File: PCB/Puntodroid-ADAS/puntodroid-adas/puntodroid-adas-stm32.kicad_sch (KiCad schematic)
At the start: 6 parts, among them J1 USB_B, J2 BOOTLOADER, J3 SWD_INTERFACE, U1 STM32F446VETx

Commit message: UPDATE cube mx
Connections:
- net CAN_LS_FAULT: no longer U1.83 (PD2)
- net SWCLK: now also U1.76 (PA14)
- net SWDIO: now also U1.72 (PA13)
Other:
- note added: "SPI1_MISO"
- note added: "SPI1_MOSI"
- note added: "SPI1_NSS"
- note added: "SPI1_SCK"

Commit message: update puntodroid
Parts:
- removed J3: SWD_INTERFACE, symbol Connector_Generic:Conn_01x06
- added C1, C2: 22p, symbol Device:C
- added C10, C12, C13, C5, C6, C7, C8, C9: 100n, symbol Device:C
- added C3, C4: 2u2, symbol Device:C_Polarized
- added J3: SWD PROGRAMMER, symbol Connector_Generic:Conn_01x05
- added R3: 5k6, symbol Device:R
- added R4, R5: 10k, symbol Device:R
- added U2: CM1293A, Package_TO_SOT_SMD:SOT-23-6, symbol Power_Protection:CDSOT236-0504C
- added Y1: 16MHz, symbol Device:Crystal
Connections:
- net +3V3: now also J2.1 (Pin_1), C10.2, C12.2, C13.2, C5.2, C6.2, C7.2, C8.2, C9.2, J3.2 (Pin_2), U2.5 (VP); no longer J2.6 (Pin_6)
- net BOOT0: now also J2.5 (Pin_5); no longer J2.2 (Pin_2)
- net BOOTLOADER_RX: now also J2.3 (Pin_3); no longer J2.4 (Pin_4)
- net BOOTLOADER_TX: now also J2.2 (Pin_2); no longer J2.5 (Pin_5)
- net CAN_LS_FAULT: now also U1.96 (PB9); no longer U1.53 (PB14)
- net CAN_LS_RX: now also U1.52 (PB13); no longer U1.51 (PB12)
- net CAN_LS_TX: now also U1.51 (PB12); no longer U1.52 (PB13)
- net DS18B20: now also U1.83 (PD2); no longer U1.24 (PA1)
- net GNDD: now also J2.6 (Pin_6), C1.1, C10.1, C12.1, C13.1, C2.1, C3.2, C4.2, C5.1, C6.1, C7.1, C8.1, C9.1, J3.3 (Pin_3), R4.2, R5.2, U2.2 (VN); no longer J2.1 (Pin_1)
- net NRST: now also J2.4 (Pin_4), J3.1 (Pin_1); no longer J2.3 (Pin_3)
- net PUSH_BUTTON_1: now also U1.5 (PE6); no longer U1.84 (PD3)
- net PUSH_BUTTON_2: now also U1.15 (PC0); no longer U1.85 (PD4)
- net PUSH_BUTTON_3: now also U1.16 (PC1); no longer U1.86 (PD5)
- net PUSH_BUTTON_4: now also U1.17 (PC2); no longer U1.87 (PD6)
- net PUSH_BUTTON_5: now also U1.18 (PC3); no longer U1.88 (PD7)
- net SWCLK: now also J3.5 (Pin_5)
- net SWDIO: now also J3.4 (Pin_4)
- net USB_D+: now also U2.4 (IO3), U2.6 (IO4)
- net USB_D-: now also U2.1 (IO1), U2.3 (IO2)
- net USB_VBUS: now also R3.2, R4.1; no longer J1.1 (VBUS)
- net VIDEO_MUX_A1: now also U1.36 (PB1); no longer U1.25 (PA2), U1.26 (PA3)
- net PE2_UNUSED: now reaches U1.1 (PE2)
- net at U1.12 (PH0): now also C1.2, Y1.2
- net at U1.13 (PH1): now also C2.2, Y1.1
- net PE3_UNUSED: now reaches U1.2 (PE3)
- net ADC_VBATT_12V: now reaches U1.23 (PA0)
- net PE4_UNUSED: now reaches U1.3 (PE4)
- net at U1.37 (PB2): now also R5.1
- net VIDEO_MUX_A2: now reaches U1.38 (PE7)
- net PE8_UNUSED: now reaches U1.39 (PE8)
- net PUSH_BUTTON_0: now reaches U1.4 (PE5)
- net PE9_UNUSED: now reaches U1.40 (PE9)
- net P10_UNUSED: now reaches U1.41 (PE10)
- net PE11_UNUSED: now reaches U1.42 (PE11)
- net PE12_UNUSED: now reaches U1.43 (PE12)
- net PE13_UNUSED: now reaches U1.44 (PE13)
- net PE14_UNUSED: now reaches U1.45 (PE14)
- net RFM69_CS: now reaches U1.46 (PE15)
- net RFM69_SCK: now reaches U1.47 (PB10)
- net at U1.48 (VCAP_1): now also C4.1
- net RFM69_MISO: now reaches U1.54 (PB15)
- net PD8_UNUSED: now reaches U1.55 (PD8)
- net PD9_UNUSED: now reaches U1.56 (PD9)
- net PD10_UNUSED: now reaches U1.57 (PD10)
- net PD11_UNUSED: now reaches U1.58 (PD11)
- net PD12_UNUSED: now reaches U1.59 (PD12)
- net PD13_UNUSED: now reaches U1.60 (PD13)
- net PD14_UNUSED: now reaches U1.61 (PD14)
- net PD15_UNUSED: now reaches U1.62 (PD15)
- net PC6_UNUSED: now reaches U1.63 (PC6)
- net PC7_UNUSED: now reaches U1.64 (PC7)
- net PC8_UNUSED: now reaches U1.65 (PC8)
- net PC9_UNUSED: now reaches U1.66 (PC9)
- net PA8_UNUSED: now reaches U1.67 (PA8)
- net PA10_UNUSED: now reaches U1.69 (PA10)
- net PC13_UNUSED: now reaches U1.7 (PC13)
- net at U1.73 (VCAP_2): now also C3.1
- net BOOTLOADER_DEBUG_RX: now reaches U1.78 (PC10)
- net BOOTLOADER_DEBUG_TX: now reaches U1.79 (PC11)
- net PC14_UNUSED: now reaches U1.8 (PC14)
- net PC12_UNUSED: now reaches U1.80 (PC12)
- net PB3_UNUSED: now reaches U1.89 (PB3)
- net PC15_UNUSED: now reaches U1.9 (PC15)
- net PB4_UNUSED: now reaches U1.90 (PB4)
- net PB5_UNUSED: now reaches U1.91 (PB5)
- net PB6_UNUSED: now reaches U1.92 (PB6)
- net PB7_UNUSED: now reaches U1.93 (PB7)
- net PB8_UNUSED: now reaches U1.95 (PB8)
- net PE0_UNUSED: now reaches U1.97 (PE0)
- net PE1_UNUSED: now reaches U1.98 (PE1)
- new net: J1.1 (VBUS), R3.1
- new net ADC_5V: U1.24 (PA1)
- new net BUZZER_OUT: U1.84 (PD3)
- new net LPGTECH_RX: U1.25 (PA2)
- new net LPGTECH_TX: U1.26 (PA3)
- new net PD5_UNUSED: U1.86 (PD5)
- new net PD6_UNUSED: U1.87 (PD6)
- new net PD7_UNUSED: U1.88 (PD7)
- new net REVERSE_SIGNAL: U1.85 (PD4)
- new net RFM69_MOSI: U1.53 (PB14)
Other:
- note added: "16MHz CRYSTAL"
- note added: "ADC_IN0"
- note added: "ADC_IN1"
- note added: "BOOT1 configuration"
- note added: "BOOTLOADER DEBUG UART"
- note added: "CAN2_RX"
- note added: "CAN2_TX"
- note added: "RCC_OSC_IN"
- note added: "RCC_OSC_OUT"
- note added: "SPI2_MISO"
- note added: "SPI2_MOSI"
- note added: "SPI2_SCK"
- note added: "SWD PROGRAMMING"
- note added: "USART2_RX"
- note added: "USART2_TX"
- note added: "USART3_RX"
- note added: "USART3_TX"
- note added: "USB SOCKET"
- moved on the sheet: J1, J2, R1

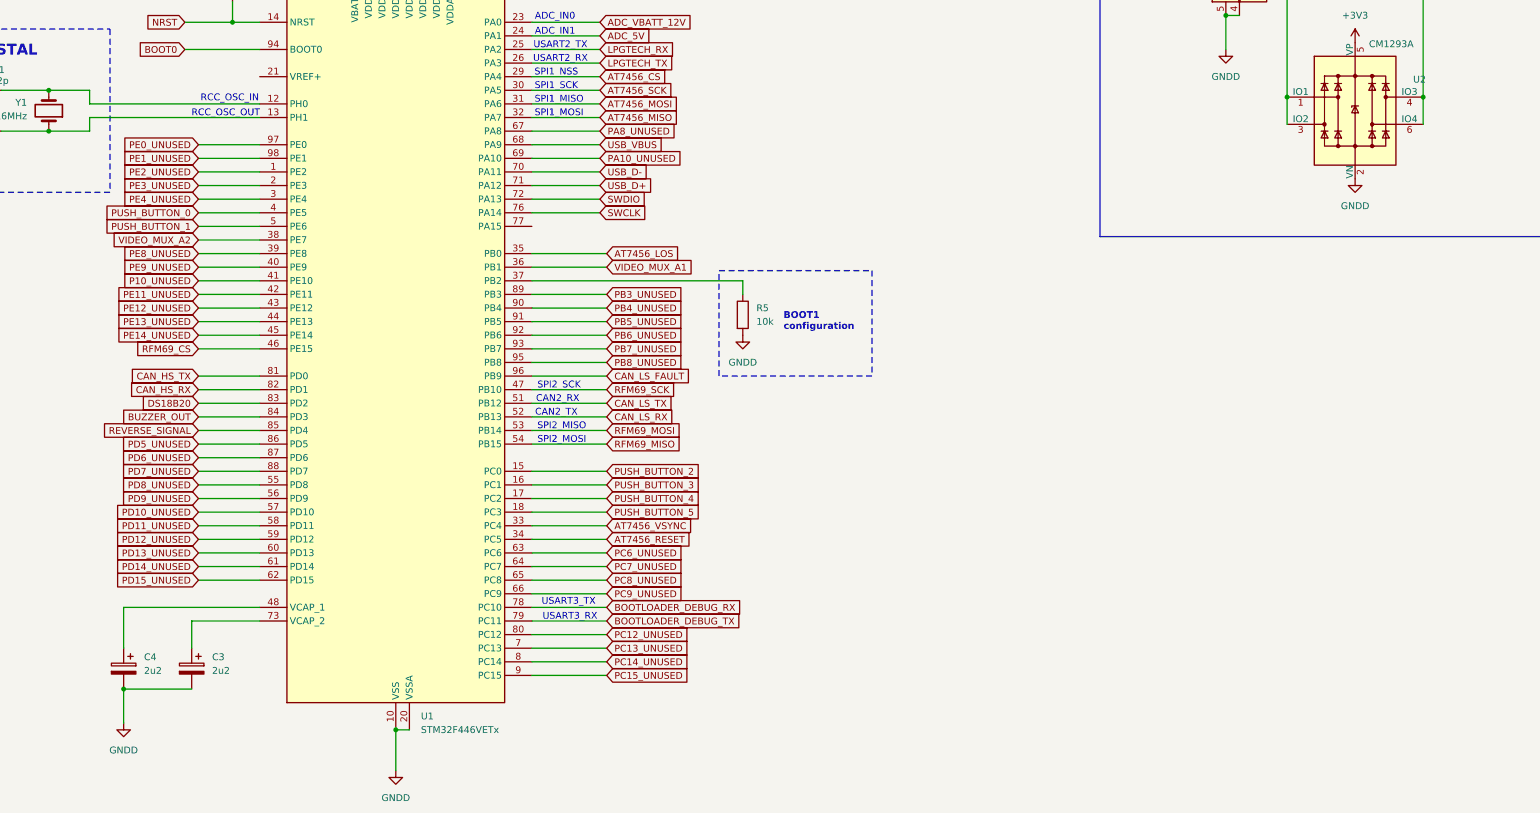
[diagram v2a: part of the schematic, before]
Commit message: update camera video path
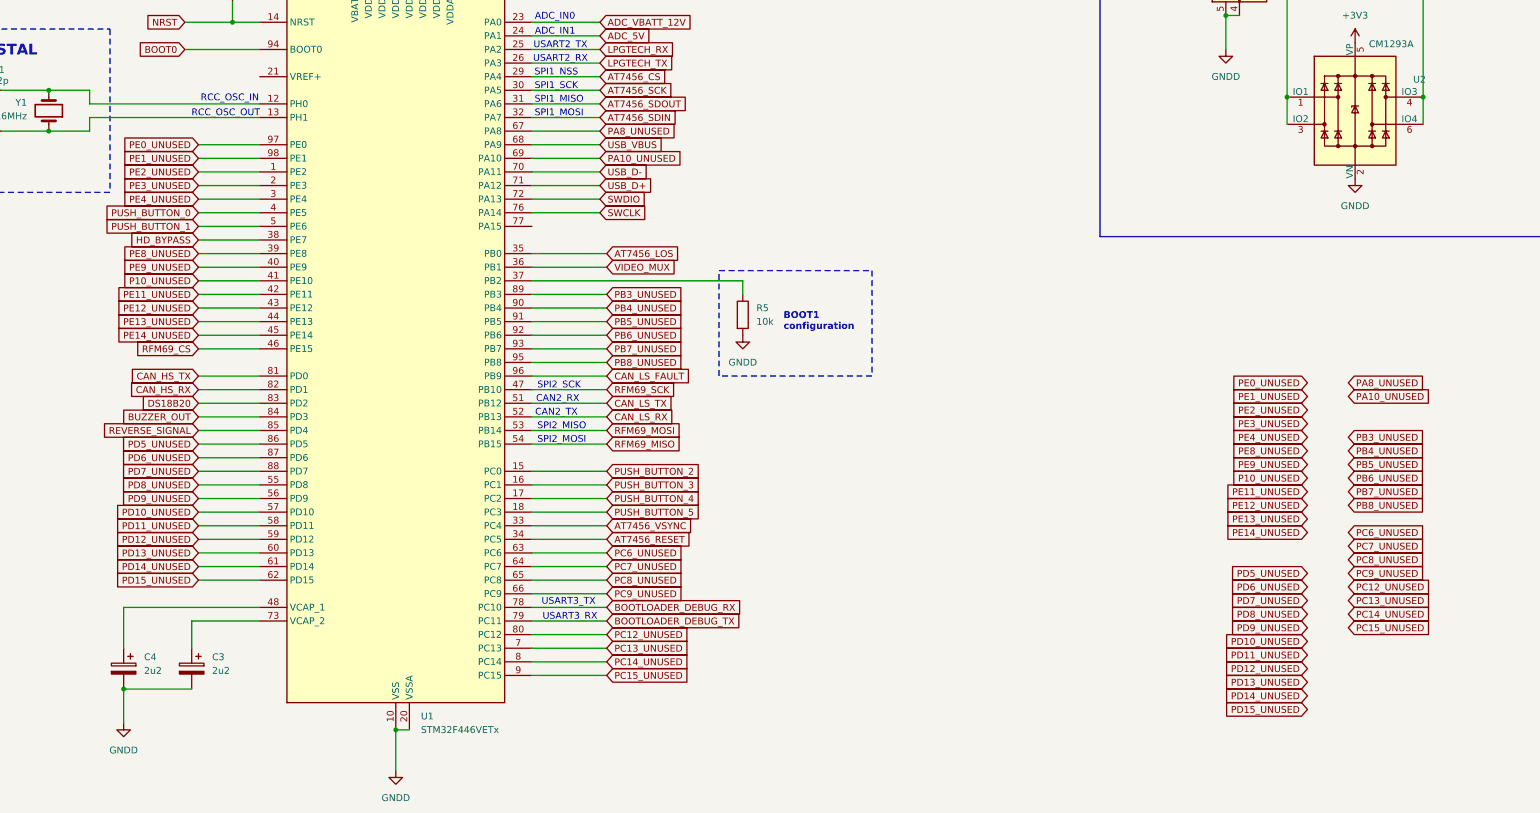
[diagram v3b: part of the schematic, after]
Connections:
- net AT7456_MISO renamed AT7456_SDIN
- net AT7456_MOSI renamed AT7456_SDOUT
- net VIDEO_MUX_A1 renamed VIDEO_MUX
- net VIDEO_MUX_A2 renamed HD_BYPASS

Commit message: update puntodroid schematic
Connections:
- net PE8_UNUSED renamed CAMERA_FRONT_EN
- net PE9_UNUSED renamed CAMERA_BACK_EN
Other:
- note added: "CAN1_RX"
- note added: "CAN1_TX"
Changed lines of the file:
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@@
 		)
 	)
+	(text "CAN1_RX"
+		(exclude_from_sim no)
+		(at 157.226 128.778 0)
+		(effects
+			(font
+				(size 1.27 1.27)
+			)
+		)
+	)
+	(text "CAN1_TX"
+		(exclude_from_sim no)
+		(at 156.972 131.318 0)
+		(effects
+			(font
+				(size 1.27 1.27)
+			)
+		)
+	)
 	(text "USB SOCKET"
 		(exclude_from_sim no)
@@
 		)
 	)
-	(global_label "PE8_UNUSED"
+	(global_label "USB_D+"
 		(shape input)
-		(at 356.87 143.51 180)
+		(at 384.81 52.07 0)
 		(fields_autoplaced yes)
 		(effects
 			(font
 				(size 1.27 1.27)
-				(thickness 0.1588)
-				(color 255 0 255 1)
 			)
-			(justify right)
+			(justify left)
 		)
 		(property "Intersheetrefs" "${INTERSHEET_REFS}"
-			(at 341.1927 143.51 0)
+			(at 395.4152 52.07 0)
 			(effects
 				(font
 					(size 1.27 1.27)
 				)
-				(justify right)
+				(justify left)
 				(hide yes)
 			)
 		)
 	)
-	(global_label "USB_D+"
+	(global_label "CAMERA_FRONT_EN"
 		(shape input)
-		(at 384.81 52.07 0)
+		(at 149.86 106.68 180)
 		(fields_autoplaced yes)
 		(effects
@@
 				(size 1.27 1.27)
 			)
-			(justify left)
+			(justify right)
 		)
 		(property "Intersheetrefs" "${INTERSHEET_REFS}"
-			(at 395.4152 52.07 0)
+			(at 136.1705 106.68 0)
 			(effects
 				(font
 					(size 1.27 1.27)
 				)
-				(justify left)
+				(justify right)
 				(hide yes)
 			)
@@
 		)
 	)
-	(global_label "PE9_UNUSED"
-		(shape input)
-		(at 356.87 146.05 180)
-		(fields_autoplaced yes)
-		(effects
-			(font
-				(size 1.27 1.27)
-				(thickness 0.1588)
-				(color 255 0 255 1)
-			)
-			(justify right)
-		)
-		(property "Intersheetrefs" "${INTERSHEET_REFS}"
-			(at 341.1927 146.05 0)
-			(effects
-				(font
-					(size 1.27 1.27)
-				)
-				(justify right)
-				(hide yes)
-			)
-		)
-	)
 	(global_label "PD14_UNUSED"
 		(shape input)
@@
 		)
 	)
-	(global_label "PE8_UNUSED"
-		(shape input)
-		(at 149.86 106.68 180)
-		(fields_autoplaced yes)
-		(effects
-			(font
-				(size 1.27 1.27)
-				(thickness 0.1588)
-				(color 255 0 255 1)
-			)
-			(justify right)
-		)
-		(property "Intersheetrefs" "${INTERSHEET_REFS}"
-			(at 134.1827 106.68 0)
-			(effects
-				(font
-					(size 1.27 1.27)
-				)
-				(justify right)
-				(hide yes)
-			)
-		)
-	)
 	(global_label "PE1_UNUSED"
 		(shape input)
@@
 	(global_label "PE14_UNUSED"
 		(shape input)
-		(at 356.87 158.75 180)
+		(at 356.87 153.67 180)
 		(fields_autoplaced yes)
 		(effects
@@
 		)
 		(property "Intersheetrefs" "${INTERSHEET_REFS}"
-			(at 341.1927 158.75 0)
+			(at 341.1927 153.67 0)
 			(effects
 				(font
@@
 	(global_label "P10_UNUSED"
 		(shape input)
-		(at 356.87 148.59 180)
+		(at 356.87 143.51 180)
 		(fields_autoplaced yes)
 		(effects
@@
 		)
 		(property "Intersheetrefs" "${INTERSHEET_REFS}"
-			(at 341.1927 148.59 0)
+			(at 341.1927 143.51 0)
 			(effects
 				(font
@@
 		)
 	)
-	(global_label "PE9_UNUSED"
-		(shape input)
-		(at 149.86 109.22 180)
-		(fields_autoplaced yes)
-		(effects
-			(font
-				(size 1.27 1.27)
-				(thickness 0.1588)
-				(color 255 0 255 1)
-			)
-			(justify right)
-		)
-		(property "Intersheetrefs" "${INTERSHEET_REFS}"
-			(at 134.1827 109.22 0)
-			(effects
-				(font
-					(size 1.27 1.27)
-				)
-				(justify right)
-				(hide yes)
-			)
-		)
-	)
 	(global_label "PA8_UNUSED"
 		(shape input)
@@
 	(global_label "PE13_UNUSED"
 		(shape input)
-		(at 356.87 156.21 180)
+		(at 356.87 151.13 180)
 		(fields_autoplaced yes)
 		(effects
@@
 		)
 		(property "Intersheetrefs" "${INTERSHEET_REFS}"
-			(at 341.1927 156.21 0)
+			(at 341.1927 151.13 0)
 			(effects
 				(font
@@
 		)
 	)
+	(global_label "CAMERA_BACK_EN"
+		(shape input)
+		(at 149.86 109.22 180)
+		(fields_autoplaced yes)
+		(effects
+			(font
+				(size 1.27 1.27)
+			)
+			(justify right)
+		)
+		(property "Intersheetrefs" "${INTERSHEET_REFS}"
+			(at 130.2439 109.22 0)
+			(effects
+				(font
+					(size 1.27 1.27)
+				)
+				(justify right)
+				(hide yes)
+			)
+		)
+	)
 	(global_label "PC12_UNUSED"
 		(shape input)
@@
 	(global_label "PE12_UNUSED"
 		(shape input)
-		(at 356.87 153.67 180)
+		(at 356.87 148.59 180)
 		(fields_autoplaced yes)
 		(effects
@@
 		)
 		(property "Intersheetrefs" "${INTERSHEET_REFS}"
-			(at 341.1927 153.67 0)
+			(at 341.1927 148.59 0)
 			(effects
 				(font
@@
 	(global_label "PE11_UNUSED"
 		(shape input)
-		(at 356.87 151.13 180)
+		(at 356.87 146.05 180)
 		(fields_autoplaced yes)
 		(effects
@@
 		)
 		(property "Intersheetrefs" "${INTERSHEET_REFS}"
-			(at 341.1927 151.13 0)
+			(at 341.1927 146.05 0)
 			(effects
 				(font

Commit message: update puntodroid schematic stm32
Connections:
- net PA15_UNUSED: now reaches U1.77 (PA15)
- net PD5_UNUSED renamed ANDROID_EN
- net PE14_UNUSED renamed RFM69_RESET
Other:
- note added: "STM32F446 MICROCONTROLLER"
- moved on the sheet: C10, C12, C13, C5, C6, C7, C8, C9

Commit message: add quick charger
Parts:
- C1: renamed from C12; footprint (none) -> Capacitor_SMD:C_0805_2012Metric_Pad1.18x1.45mm_HandSolder
- C10: renamed from C2; footprint (none) -> Capacitor_SMD:C_0805_2012Metric_Pad1.18x1.45mm_HandSolder
- C11: renamed from C4; footprint (none) -> Capacitor_SMD:C_0805_2012Metric_Pad1.18x1.45mm_HandSolder
- C12: renamed from C3; footprint (none) -> Capacitor_SMD:C_0805_2012Metric_Pad1.18x1.45mm_HandSolder
- C2: renamed from C13; footprint (none) -> Capacitor_SMD:C_0805_2012Metric_Pad1.18x1.45mm_HandSolder
- C3: renamed from C7; footprint (none) -> Capacitor_SMD:C_0805_2012Metric_Pad1.18x1.45mm_HandSolder
- C4: renamed from C6; footprint (none) -> Capacitor_SMD:C_0805_2012Metric_Pad1.18x1.45mm_HandSolder
- C5: footprint (none) -> Capacitor_SMD:C_0805_2012Metric_Pad1.18x1.45mm_HandSolder
- C6: renamed from C8; footprint (none) -> Capacitor_SMD:C_0805_2012Metric_Pad1.18x1.45mm_HandSolder
- C7: renamed from C9; footprint (none) -> Capacitor_SMD:C_0805_2012Metric_Pad1.18x1.45mm_HandSolder
- C8: renamed from C10; footprint (none) -> Capacitor_SMD:C_0805_2012Metric_Pad1.18x1.45mm_HandSolder
- C9: renamed from C1; footprint (none) -> Capacitor_SMD:C_0805_2012Metric_Pad1.18x1.45mm_HandSolder
- J1: renamed from J3; footprint (none) -> My-Footprints-connectors:JST_XH_B5B-XH-A_1x05_P2.54mm_Vertical
- J2: footprint (none) -> My-Footprints-connectors:JST_XH_B6B-XH-A_1x06_P2.50mm_Vertical
- R1, R2: footprint (none) -> Resistor_SMD:R_0805_2012Metric_Pad1.20x1.40mm_HandSolder
- R3: renamed from R5; footprint (none) -> Resistor_SMD:R_0805_2012Metric_Pad1.20x1.40mm_HandSolder
- R4: renamed from R3; footprint (none) -> Resistor_SMD:R_0805_2012Metric_Pad1.20x1.40mm_HandSolder
- R5: renamed from R4; footprint (none) -> Resistor_SMD:R_0805_2012Metric_Pad1.20x1.40mm_HandSolder
- renumbered J1 to J3
